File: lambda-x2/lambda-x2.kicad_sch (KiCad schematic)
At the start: 102 parts, among them J1 FTSH-107-01-F-DV-K, J3 Conn_02x02_Odd_Even, J4 Conn_01x10, P1 33311-24AW-2, Q1 BTS3028, Q2 BTS3028, Q3 BTS3028, Q4 BTS3028, U2 STM32F103C6Tx, U4 LM78M05_TO252, U5 XC6206P332MR, U6 REF3033, U7 MCP6002T-I/SN, U8 TJA1051T-3

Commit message: Progress
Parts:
- added H1, H3, H4: MountingHole_Pad, symbol Mechanical:MountingHole_Pad
- added H2: (no value), symbol Mechanical:MountingHole_Pad
- R34: value (none) -> 3.3k; footprint (none) -> Resistor_SMD:R_0402_1005Metric
- U17: value (none) -> MCP6002T-I/SN; footprint (none) -> Package_SO:SO-8_3.9x4.9mm_P1.27mm
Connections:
- net GND: now also H1.1, H2.1, H3.1, H4.1
- net SPI1_CS0: now also U2.6 (PD1); no longer U2.5 (PD0)
- net SPI1_CS1: now also U2.5 (PD0); no longer U2.6 (PD1)
- net SPI1_CS2: now also U2.2 (PC13); no longer U2.38 (PA15)
- net config0: now also U2.3 (PC14); no longer U2.2 (PC13)
- net config1: now also U2.4 (PC15); no longer U2.3 (PC14)
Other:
- sheet LSU analog left ports: added none; removed Vm_sense
- sheet LSU analog right ports: added none; removed Vm_sense
- note added: "also used to measure battery voltage"
- note added: "weak!"

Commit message: Progress
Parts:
- added C12: 1u, Capacitor_SMD:C_0402_1005Metric, symbol Device:C
- added C19, C68, C69: 100n, Capacitor_SMD:C_0402_1005Metric, symbol Device:C
- added D23, D24, D25, D26: DF2B7AFS,L3M, Diode_SMD:D_SOD-923, symbol Diode:ESD9B5.0ST5G
- added D29: GREEN, LED_SMD:LED_0603_1608Metric, symbol Device:LED
- added L5: 470R@100MHz, Inductor_SMD:L_0603_1608Metric, symbol Device:L
- added R104: 1k, Resistor_SMD:R_0402_1005Metric, symbol Device:R
- added R46, R51: 1K, Resistor_SMD:R_0603_1608Metric, symbol Device:R
- added TP24, TP7, TP8, TP9: (no value), symbol Connector:TestPoint_Probe
- added U18: JDY-33, local:JDY-33, symbol JDY-33:JDY-33
- H1, H3, H4: footprint (none) -> MountingHole:MountingHole_2.5mm_Pad_Via
- H2: value (none) -> MountingHole_Pad; footprint (none) -> MountingHole:MountingHole_2.5mm_Pad_Via
- J1: now left out of the parts list
- R40: value 0R -> 1K; footprint Resistor_SMD:R_0402_1005Metric -> Resistor_SMD:R_0603_1608Metric; LCSC C325377 -> C21190; now left out of the parts list
- R50: value 10k -> 1K; footprint Resistor_SMD:R_0402_1005Metric -> Resistor_SMD:R_0603_1608Metric; LCSC C25744 -> C21190
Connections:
- net +3V3: now also J4.9 (Pin_9), C12.1, C19.1, C69.1, L5.2, TP8.1, U18.12 (3V3); no longer R50.2
- net +5V: now also R50.1, C68.1, R51.1, TP7.1
- net GND: now also C12.2, C19.2, C68.2, C69.2, D23.2 (A2), D24.2 (A2), D25.2 (A2), D26.2 (A2), R104.1, R46.2, TP24.1, U18.13 (GND)
- net I2C1_SDA: now also J4.7 (Pin_7); no longer J4.9 (Pin_9)
- net L_AUX: now also R40.1, R50.2
- net L_Ip_sense: now also U2.14 (PA4); no longer U2.15 (PA5)
- net L_OUT_en: now also U2.6 (PD1)
- net L_Un_3x_sense: now also U2.15 (PA5); no longer U2.16 (PA6)
- net L_heater_pwm: now also U2.43 (PB7); no longer U2.42 (PB6)
- net R_AUX: now also R46.1, R51.2
- net R_AUX_ADC: now also U2.16 (PA6); no longer U2.10 (PA0)
- net R_Ip_sense: now also U2.10 (PA0); no longer U2.13 (PA3)
- net R_OUT_en: now also U2.5 (PD0)
- net R_Un_3x_sense: now also U2.13 (PA3); no longer U2.14 (PA4)
- net R_heater_pwm: now also U2.42 (PB6); no longer U2.43 (PB7)
- net SPI1_CS0: now also U2.4 (PC15); no longer U2.6 (PD1)
- net SPI1_CS1: now also U2.3 (PC14); no longer U2.5 (PD0)
- net SPI1_CS2: now also J4.3 (Pin_3), U2.38 (PA15); no longer J4.7 (Pin_7), U2.2 (PC13)
- net UART_RX: now also U18.1 (TXD)
- net UART_TX: now also U18.2 (RXD)
- net VDDA: now also L5.1, TP9.1
- net config0: now also U2.2 (PC13); no longer U2.3 (PC14)
- net at R35.1, R37.2, U7.1: now also D26.1 (A1)
- net at R31.1, R32.2, U7.7: now also D25.1 (A1)
- net at R96.1, U17.5 (+): now also D23.1 (A1)
- net at R97.1, U17.3 (+): now also D24.1 (A1)
- removed net config1: R40.1, R50.1, U2.4 (PC15)
- new net: D29.1 (K), R104.2
- new net: D29.2 (A), U18.16 (ALED)
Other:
- note added: "DNI"
- moved on the sheet: C1, C38, C39, C4, C40, C41, C5, C6, D1, D2, H1, H2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

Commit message: cosmetic
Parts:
- TP24: value (none) -> GND; footprint (none) -> TestPoint:TestPoint_Pad_D1.0mm
- TP7: value (none) -> 5V; footprint (none) -> TestPoint:TestPoint_Pad_D1.0mm
- TP8: value (none) -> 3V3; footprint (none) -> TestPoint:TestPoint_Pad_D1.0mm
- TP9: value (none) -> Vdda; footprint (none) -> TestPoint:TestPoint_Pad_D1.0mm
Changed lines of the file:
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@@
       (effects (font (size 1.27 1.27)) (justify left) hide)
     )
-    (property "Value" "" (id 1) (at 383.54 58.42 0)
-      (effects (font (size 1.27 1.27)) (justify left))
-    )
-    (property "Footprint" "" (id 2) (at 386.08 62.23 0)
+    (property "Value" "GND" (id 1) (at 383.54 58.42 0)
+      (effects (font (size 1.27 1.27)) (justify left))
+    )
+    (property "Footprint" "TestPoint:TestPoint_Pad_D1.0mm" (id 2) (at 386.08 62.23 0)
       (effects (font (size 1.27 1.27)) hide)
     )
@@
       (effects (font (size 1.27 1.27)) (justify left) hide)
     )
-    (property "Value" "" (id 1) (at 365.76 30.48 0)
-      (effects (font (size 1.27 1.27)) (justify left))
-    )
-    (property "Footprint" "" (id 2) (at 368.3 34.29 0)
+    (property "Value" "3V3" (id 1) (at 365.76 30.48 0)
+      (effects (font (size 1.27 1.27)) (justify left))
+    )
+    (property "Footprint" "TestPoint:TestPoint_Pad_D1.0mm" (id 2) (at 368.3 34.29 0)
       (effects (font (size 1.27 1.27)) hide)
     )
@@
       (effects (font (size 1.27 1.27)) (justify left) hide)
     )
-    (property "Value" "" (id 1) (at 326.39 30.48 0)
-      (effects (font (size 1.27 1.27)) (justify left))
-    )
-    (property "Footprint" "" (id 2) (at 328.93 34.29 0)
+    (property "Value" "5V" (id 1) (at 326.39 30.48 0)
+      (effects (font (size 1.27 1.27)) (justify left))
+    )
+    (property "Footprint" "TestPoint:TestPoint_Pad_D1.0mm" (id 2) (at 328.93 34.29 0)
       (effects (font (size 1.27 1.27)) hide)
     )
@@
       (effects (font (size 1.27 1.27)) (justify left) hide)
     )
-    (property "Value" "" (id 1) (at 365.76 58.42 0)
-      (effects (font (size 1.27 1.27)) (justify left))
-    )
-    (property "Footprint" "" (id 2) (at 368.3 62.23 0)
-      (effects (font (size 1.27 1.27)) hide)
-    )
+    (property "Value" "Vdda" (id 1) (at 365.76 58.42 0)
+      (effects (font (size 1.27 1.27)) (justify left))
+    )
+    (property "Footprint" "TestPoint:TestPoint_Pad_D1.0mm" (id 2) (at 368.3 62.23 0)
+      (effects (font (size 1.27 1.27)) hide)
+    )

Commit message: Progress
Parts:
- removed TP1, TP2: TestPoint, Connector_PinHeader_2.54mm:PinHeader_1x01_P2.54mm_Vertical, symbol Connector:TestPoint
- added JP1, JP3: (no value), symbol Jumper:SolderJumper_2_Open
- added JP2: SolderJumper_2_Open, Jumper:SolderJumper-2_P1.3mm_Open_TrianglePad1.0x1.5mm, symbol Jumper:SolderJumper_2_Open
- added TP25, TP26, TP27: (no value), symbol Connector:TestPoint_Probe
- Q2: value BTS3028 -> (none); footprint Package_TO_SOT_SMD:TO-252-2 -> (none)
- R39: value 0R -> (none); footprint Resistor_SMD:R_0402_1005Metric -> (none); now left out of the parts list
- R98, R99: value 82k -> (none)
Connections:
- net +3V3: now also JP3.1 (A)
- net +5V: now also JP1.2 (B)
- net Boot0: now also JP3.2 (B)
- net GND: now also JP2.1 (A)
- net L_AUX: now also JP1.1 (A)
- net SPI1_CS0: now also TP25.1
- net SPI1_CS1: now also TP26.1
- net nRESET: now also JP2.2 (B)
- net at C21.1, C22.1, D6.1 (K)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: now also TP27.1
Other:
- note added: "1.524x div"
- note added: "2x analog inputs"
- note added: "Enable 5V output"
- moved on the sheet: D1, D2, D29, R10, R104, R16, R23, R8

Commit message: Progress
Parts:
- H1, H2, H3, H4: value MountingHole_Pad -> (none); footprint MountingHole:MountingHole_2.5mm_Pad_Via -> (none); now left out of the parts list
- JP1, JP3: value (none) -> SolderJumper_2_Open; footprint (none) -> Jumper:SolderJumper-2_P1.3mm_Open_TrianglePad1.0x1.5mm
- Q2: value (none) -> BTS3028; footprint (none) -> Package_TO_SOT_SMD:TO-252-2
- R39: value (none) -> 0R; footprint (none) -> Resistor_SMD:R_0402_1005Metric
- R98, R99: value (none) -> 82k
- TP25: value (none) -> CS0; footprint (none) -> TestPoint:TestPoint_Pad_D1.0mm
- TP26: value (none) -> CS1; footprint (none) -> TestPoint:TestPoint_Pad_D1.0mm
- TP27: value (none) -> 12V prot; footprint (none) -> TestPoint:TestPoint_Pad_D1.0mm

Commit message: Replace DF2B7AFS,L3M to ESD5V0D9B, fix mcp6002 LCSC
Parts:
- D23, D24, D25, D26: value DF2B7AFS,L3M -> ESD5V0D9B; LCSC C1972965 -> C484329
- H1, H2, H3, H4: value (none) -> MountingHole_Pad; footprint (none) -> MountingHole:MountingHole_2.5mm_Pad_Via
- U17, U7: value MCP6002T-I/SN -> (none); footprint Package_SO:SO-8_3.9x4.9mm_P1.27mm -> (none)

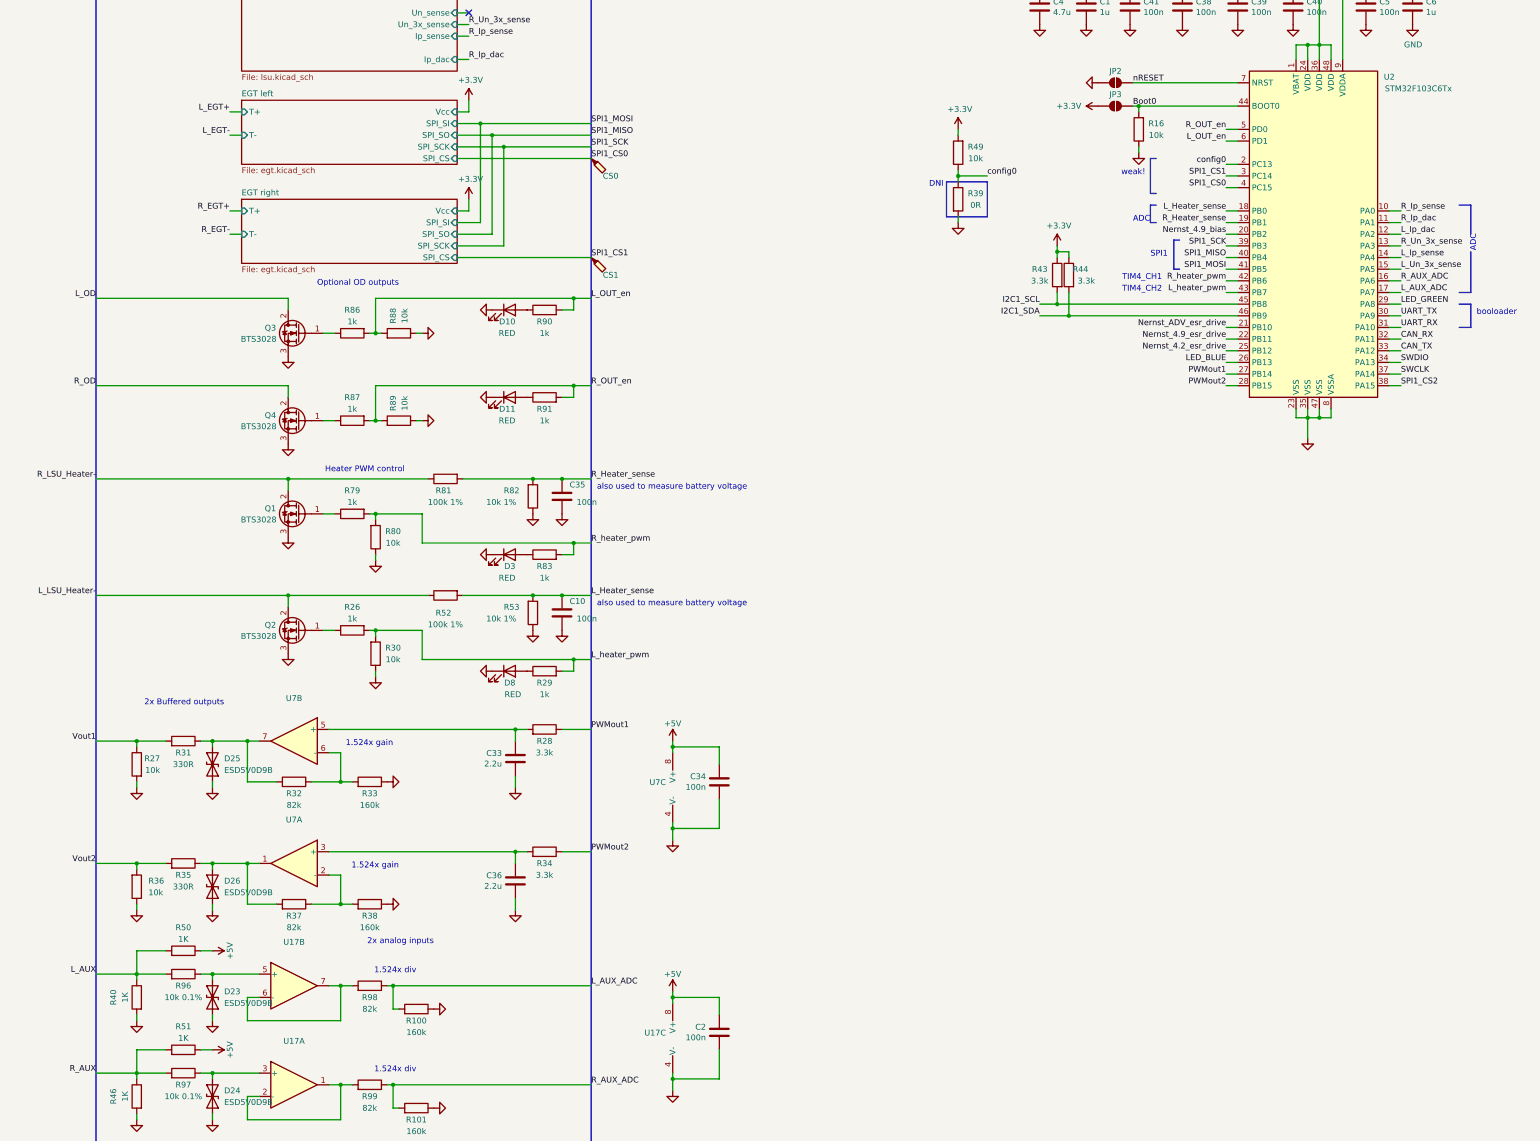
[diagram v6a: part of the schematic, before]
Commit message: lambda-x2: revork aux outputs, remove useless protection in LSU
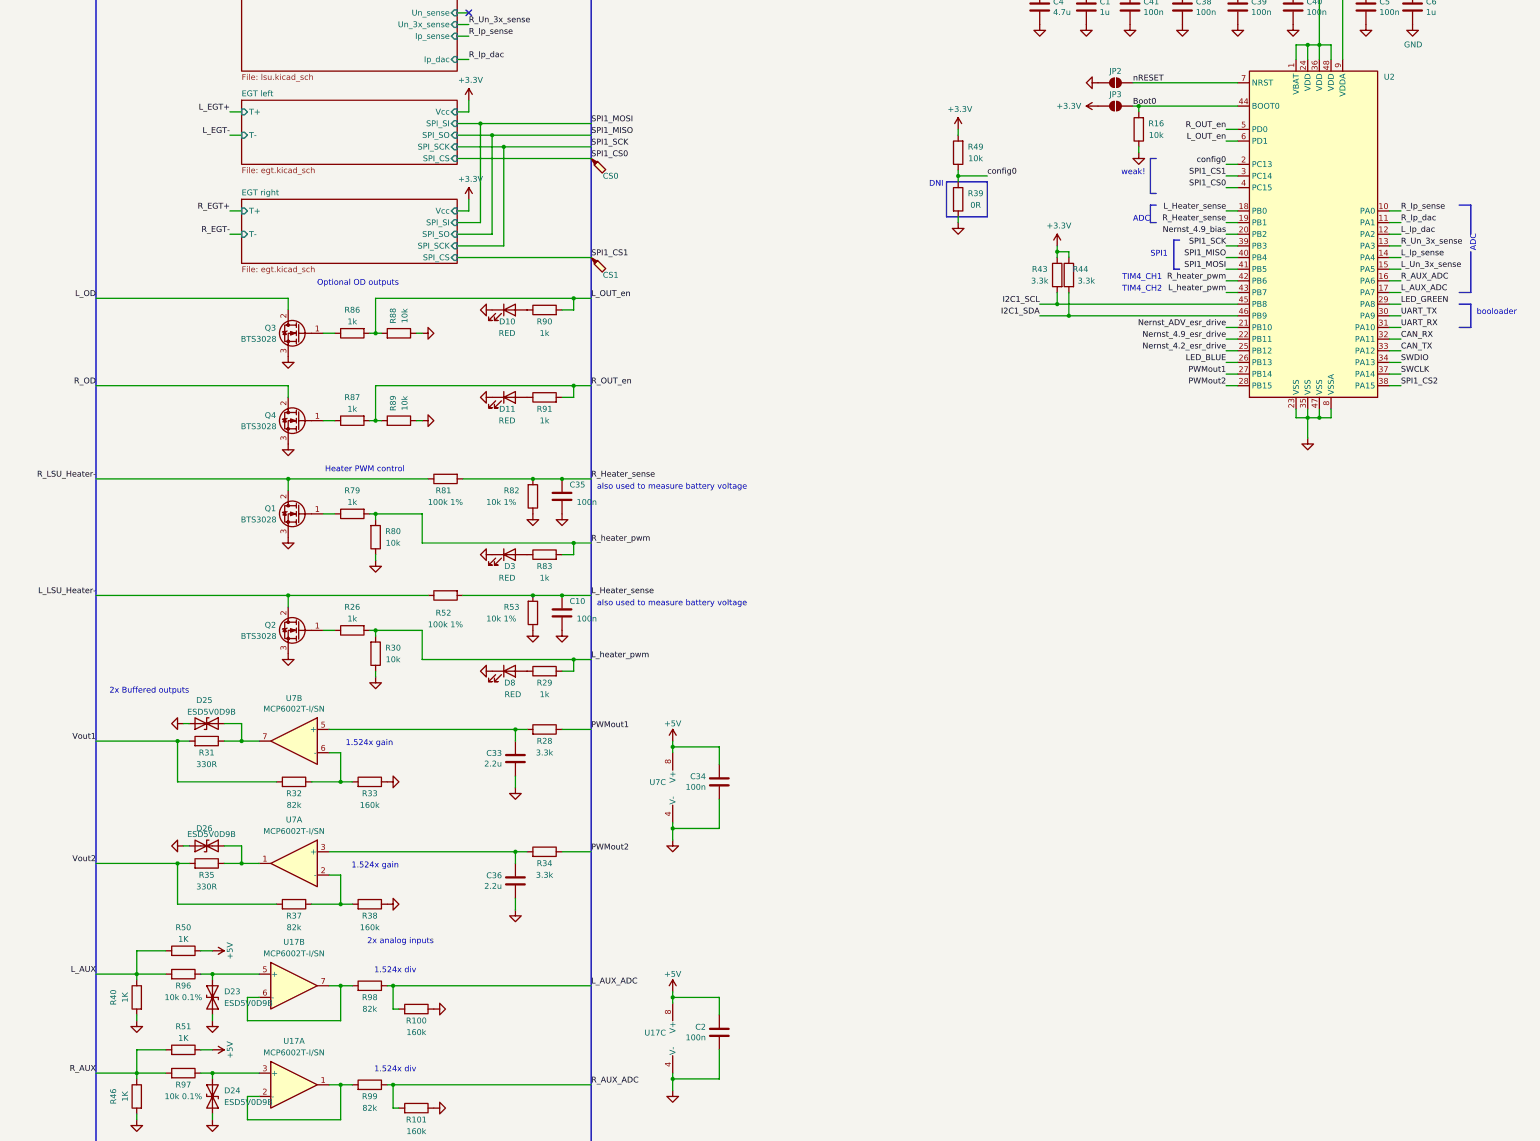
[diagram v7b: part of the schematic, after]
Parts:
- removed R27, R36: 10k, Resistor_SMD:R_0402_1005Metric, symbol Device:R
- U17, U7: value (none) -> MCP6002T-I/SN; footprint (none) -> Package_SO:SOIC-8_3.9x4.9mm_P1.27mm
- U2: value STM32F103C6Tx -> (none); footprint Package_QFP:LQFP-48_7x7mm_P0.5mm -> (none)
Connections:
- net Vout1: now also R32.2
- net Vout2: now also R37.2
- net at D26.1 (A1), R35.1, U7.1: no longer R37.2
- net at D25.1 (A1), R31.1, U7.7: no longer R32.2
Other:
- moved on the sheet: D25, D26, R31, R35
